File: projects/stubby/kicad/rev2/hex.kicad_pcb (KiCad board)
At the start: 2 copper layers, 49.5 x 49.5 mm, 60 parts, among them IC1 ATMEGA1284-A, P1 BATT (4.8V-6V), P10 CONN_4, P11 CONN_4, P2 PROG, P3 CONN_10, P4 CONN_6, P5 CONN_13, P6 CONN_6, P7 CONN_1, P8 CONN_6, P9 CONN_2, SW1 DPDT, X1 CRYSTAL_RESONATOR

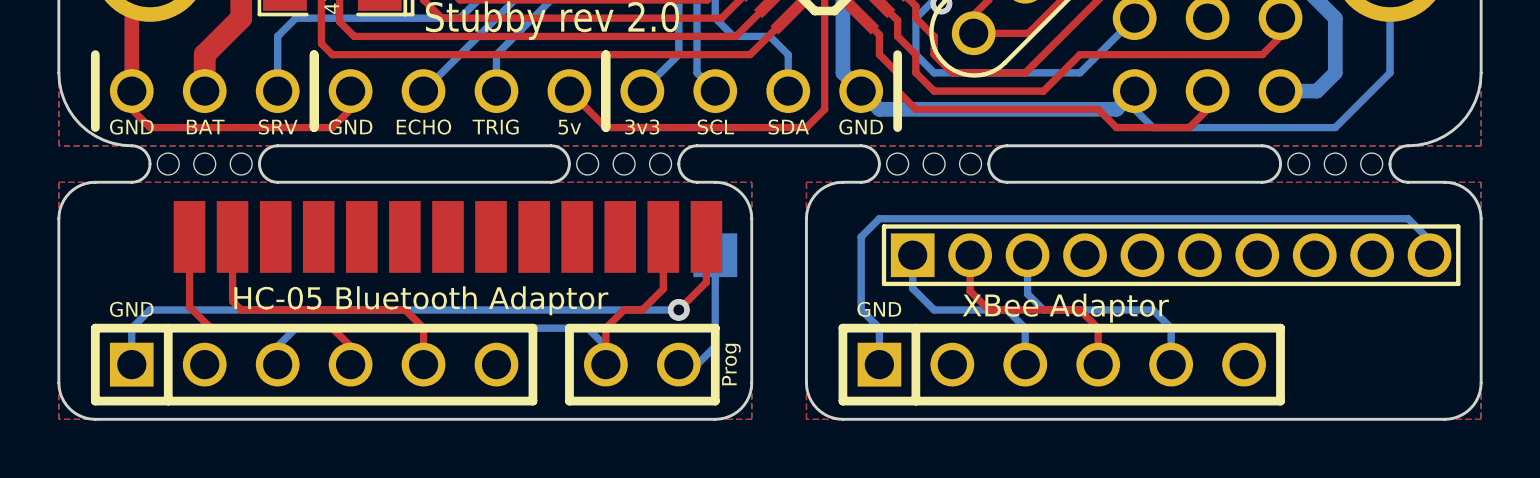
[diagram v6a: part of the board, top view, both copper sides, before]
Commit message: Adjusted rev2 breakout boards to fit better on the board; verification and possibly more work still required.
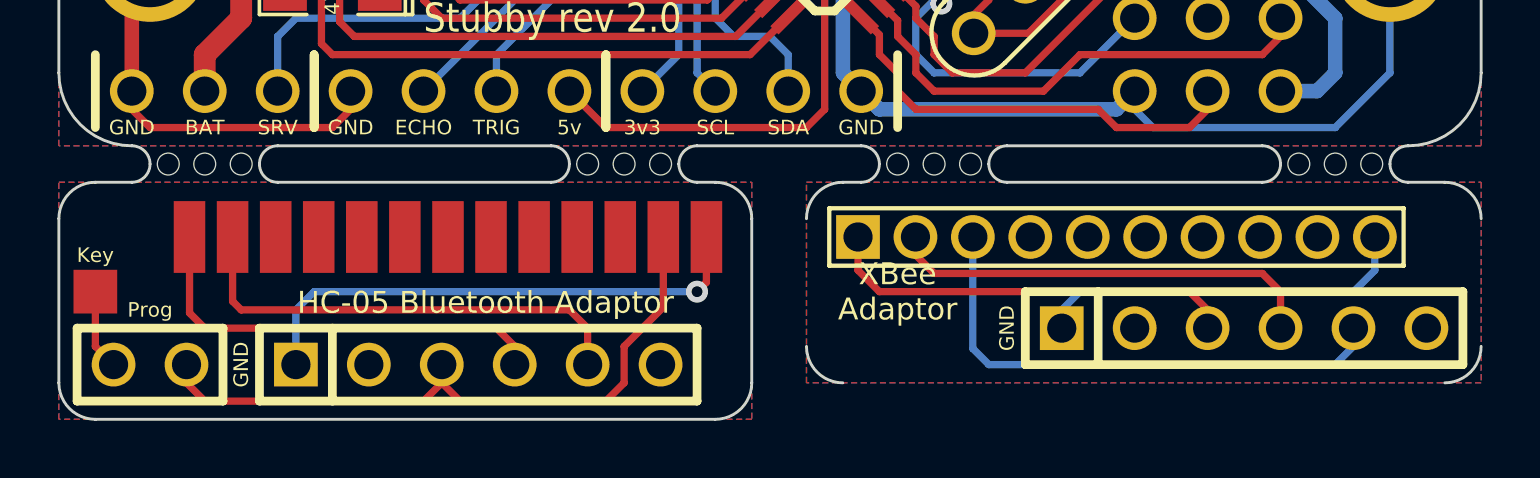
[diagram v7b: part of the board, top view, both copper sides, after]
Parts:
- P7: moved to F.Cu
- moved P7 21.6 mm to (36.8, 59.7)
- moved P9 17.1 mm to (38.7, 62.2), turned to 0 degrees
- moved P4 6.48 mm to (76.8, 61.0)
- moved P8 5.71 mm to (50.2, 62.2)
- moved P3 2.01 mm to (72.4, 57.8)
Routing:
- net /XBEE_GND: track 25.6 -> 13.3 mm
- net N-000005: track 8.11 -> 18.3 mm
- net N-000009: track 7.52 -> 15.1 mm
- net N-0000010: track 6.92 -> 14.5 mm
- net N-000003: track 9.25 -> 15.1 mm
- net N-000002: track 10.5 -> 16.3 mm
- net /BLUETOOTH_GND: track 23.5 -> 18.2 mm
- net N-000008: track 18.9 -> 23.2 mm
- net N-000007: track 4.71 -> 2.80 mm
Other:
- outline, holes or cut-outs redrawn

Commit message: Reversed side for key
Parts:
- P7: moved to B.Cu
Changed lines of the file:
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@@
-(kicad_pcb (version 3) (host pcbnew "(2013-dec-23)-stable")
+(kicad_pcb (version 3) (host pcbnew "(2014-01-10 BZR 4027)-stable")
   (general
     (links 163)
@@
     )
   )
-  (module SIL-1 (layer F.Cu)
+  (module SIL-1 (layer B.Cu)
     (at 36.83 59.69)
     (descr "Connecteurs 1 pin")
     (tags "CONN DEV")
-    (fp_text reference P7 (at 0 -1.7) (layer F.SilkS) hide
-      (effects (font (size 0.8 0.8) (thickness 0.15)))
+    (fp_text reference P7 (at 0 1.7) (layer B.SilkS) hide
+      (effects (font (size 0.8 0.8) (thickness 0.15)) (justify mirror))
     )
-    (fp_text value CONN_1 (at 0.1 -1.7) (layer F.SilkS) hide
-      (effects (font (size 0.8 0.8) (thickness 0.15)))
+    (fp_text value CONN_1 (at 0.1 1.7) (layer B.SilkS) hide
+      (effects (font (size 0.8 0.8) (thickness 0.15)) (justify mirror))
     )
     (pad 1 smd rect (at 0 0) (size 1.524 1.524)
-      (layers F.Cu F.Paste F.Mask)
+      (layers B.Cu B.Paste B.Mask)
       (net 56 N-000007)
     )
@@
     (effects (font (size 0.508 0.508) (thickness 0.127)))
   )
-  (gr_text Key (at 36.83 58.42) (layer F.SilkS)
-    (effects (font (size 0.508 0.508) (thickness 0.127)))
+  (gr_text Key (at 36.83 58.42) (layer B.SilkS)
+    (effects (font (size 0.508 0.508) (thickness 0.127)) (justify mirror))
   )
   (gr_arc (start 82.55 52.07) (end 85.09 52.07) (angle 90) (layer Edge.Cuts) (width 0.1))
@@
   (segment (start 60.445 24.13) (end 60.445 23.0575) (width 0.762) (layer F.Cu) (net 55))
   (segment (start 60.445 23.0575) (end 62.5475 20.955) (width 0.762) (layer F.Cu) (net 55) (status 20))
-  (segment (start 36.83 59.69) (end 36.83 61.595) (width 0.254) (layer F.Cu) (net 56))
-  (segment (start 36.83 61.595) (end 37.465 62.23) (width 0.254) (layer F.Cu) (net 56))
+  (segment (start 36.83 59.69) (end 36.83 61.595) (width 0.254) (layer B.Cu) (net 56) (status 400000))
+  (segment (start 36.83 61.595) (end 37.465 62.23) (width 0.254) (layer B.Cu) (net 56) (status 800000))
   (segment (start 48.895 62.23) (end 48.895 62.865) (width 0.254) (layer F.Cu) (net 57))
   (segment (start 48.895 62.865) (end 49.53 63.5) (width 0.254) (layer F.Cu) (net 57))
